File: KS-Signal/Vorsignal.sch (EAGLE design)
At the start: 10 parts

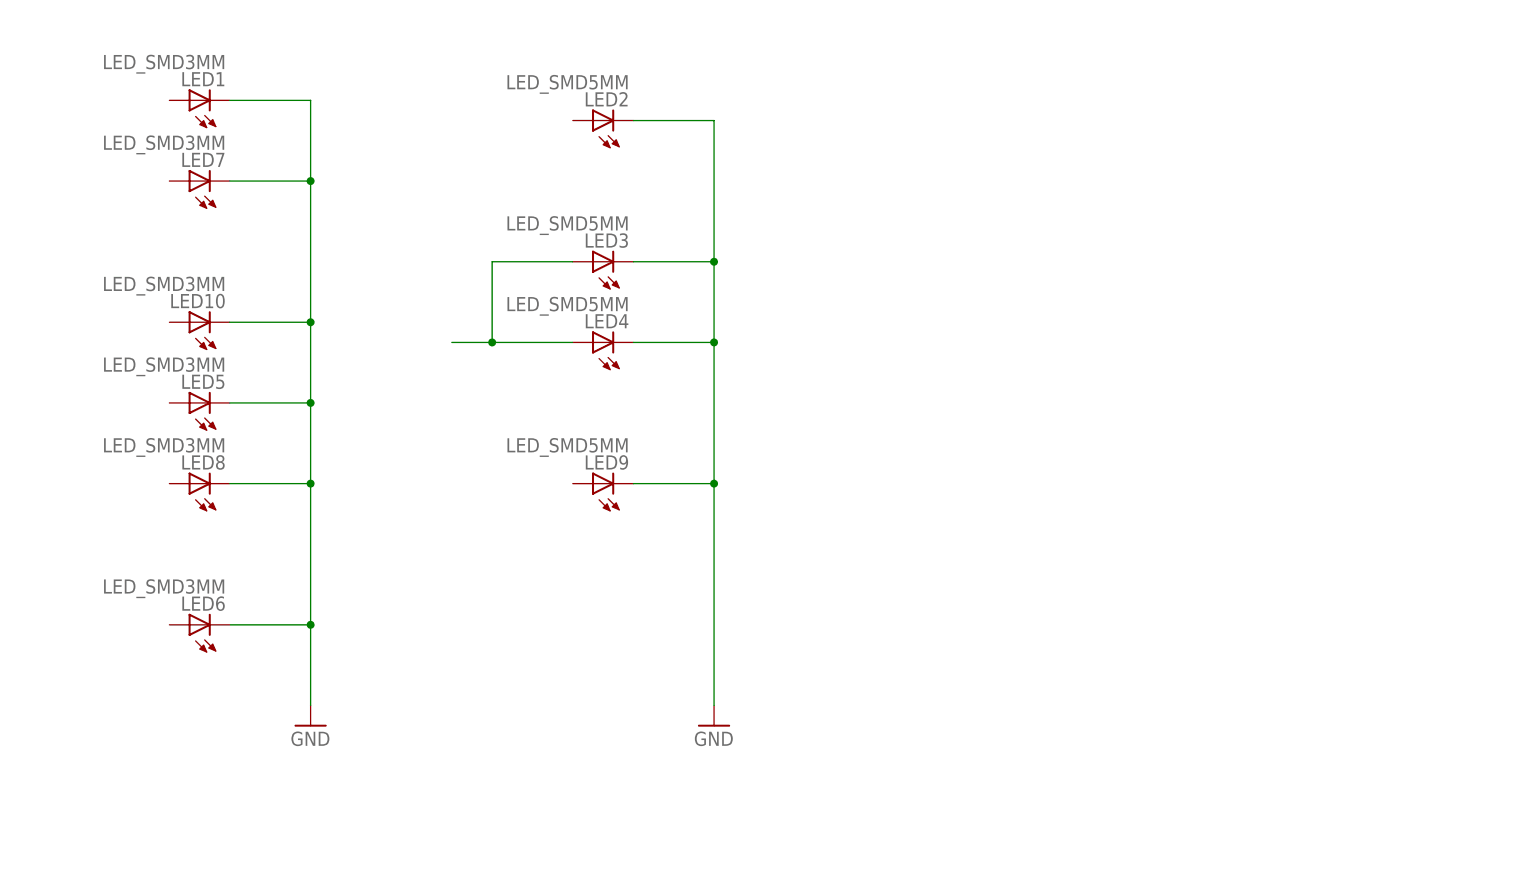
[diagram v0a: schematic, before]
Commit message: Vorsignale fertiggestellt
- Vorsignalschirme fertiggestellt
- Platinengrößen angepasst
-> Achtung: Stecker und Pinbelegung unterschiedlich zwischen den beiden Vorsignaltypen
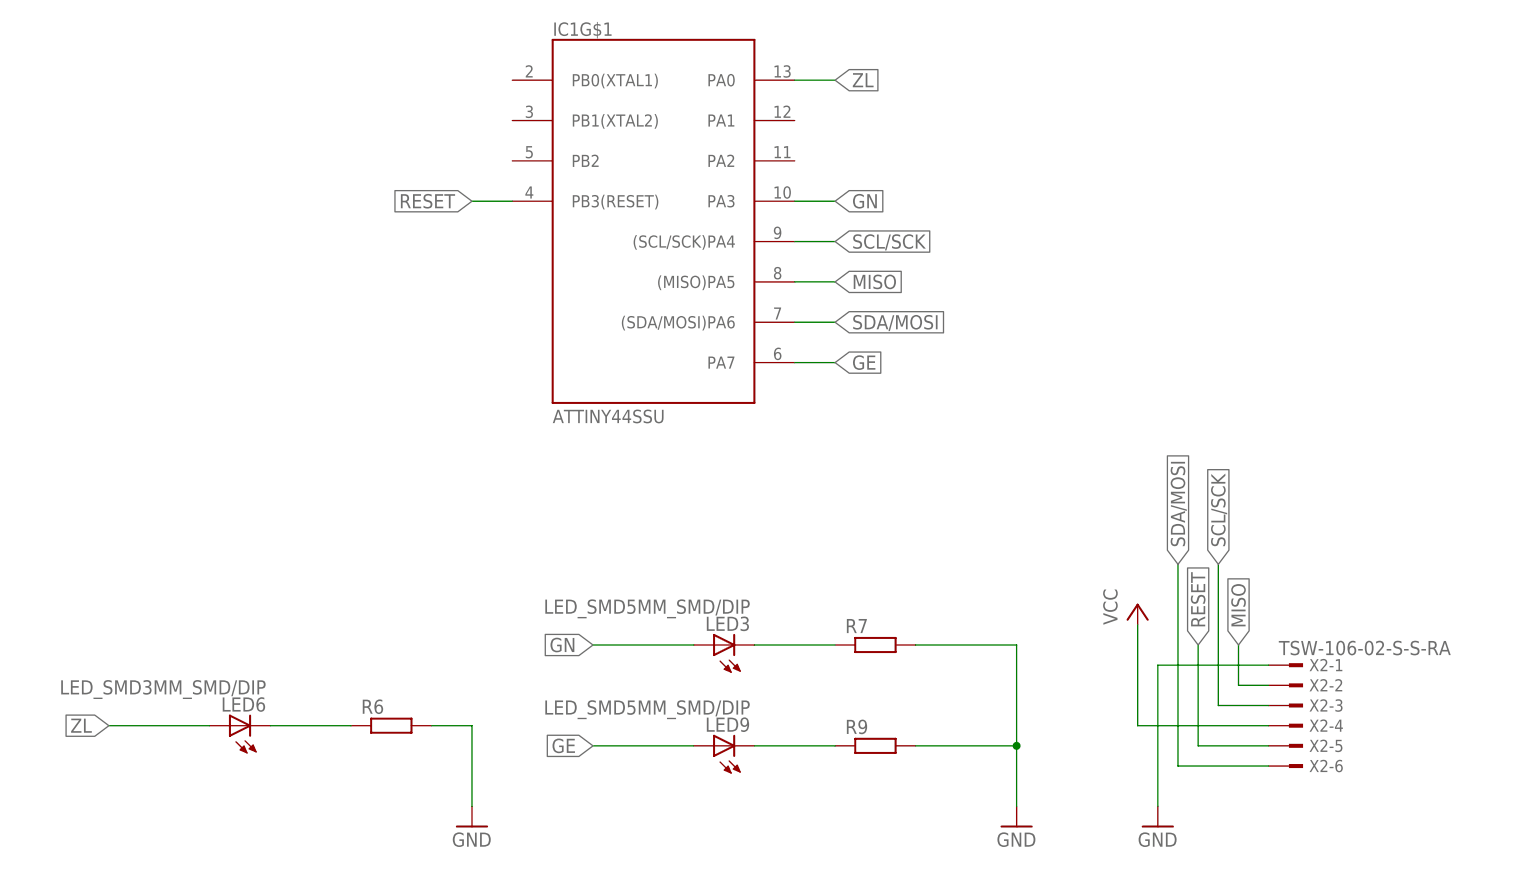
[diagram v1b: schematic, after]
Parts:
- removed LED1, LED10, LED5, LED7, LED8: LED_SMD3MM, LEDFLATTOP:LED_SMD3MM
- removed LED2, LED4: LED_SMD5MM, LEDFLATTOP:LED_SMD5MM
- added IC1: ATTINY44SSU, Attiny:ATTINY44SSU
- added R6, R7, R9: (no value), rcl:R-EU_R0603
- added X2: TSW-106-02-S-S-RA, con-samtec:TSW-106-02-S-S-RA
- LED3, LED9: value LED_SMD5MM -> LED_SMD5MM_SMD/DIP; device LEDFLATTOP:LED_SMD5MM -> LEDFLATTOP:LED_SMD5MM_SMD/DIP
- LED6: value LED_SMD3MM -> LED_SMD3MM_SMD/DIP; device LEDFLATTOP:LED_SMD3MM -> LEDFLATTOP:LED_SMD3MM_SMD/DIP
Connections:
- new net GE: IC1G$1.PA7, LED9.A
- new net GN: IC1G$1.PA3, LED3.A
- new net MISO: IC1G$1.(MISO)PA5, X2-2.1
- new net N$2: LED6.C, R6.1
- new net N$8: LED3.C, R7.1
- new net RESET: IC1G$1.PB3(RESET), X2-5.1
- new net SCL/SCK: IC1G$1.(SCL/SCK)PA4, X2-3.1
- new net SDA/MOSI: IC1G$1.(SDA/MOSI)PA6, X2-6.1
- new net VCC: X2-4.1
- new net ZL: IC1G$1.PA0, LED6.A
- net GND: now also R6.2, R7.2, R9.2, X2-1.1; no longer LED1.C, LED10.C, LED2.C, LED3.C, LED4.C, LED5.C, LED6.C, LED7.C, LED8.C, LED9.C
- net N$1: now also LED9.C, R9.1; no longer LED3.A, LED4.A
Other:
- moved on the sheet: LED3, LED6, LED9
